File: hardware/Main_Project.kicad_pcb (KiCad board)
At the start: 2 copper layers, 246.8 x 135.9 mm, 64 parts, among them J1 Motors_R, J10 BBBBBBBONUSROUND, J11 Power_Distro, J12 Power_Distro, J13 Power_Distro, J14 Power_Distro, J15 Color_Sensor, J16 Color_Sensor, J2 Motors_L, J3 Power_Outputs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

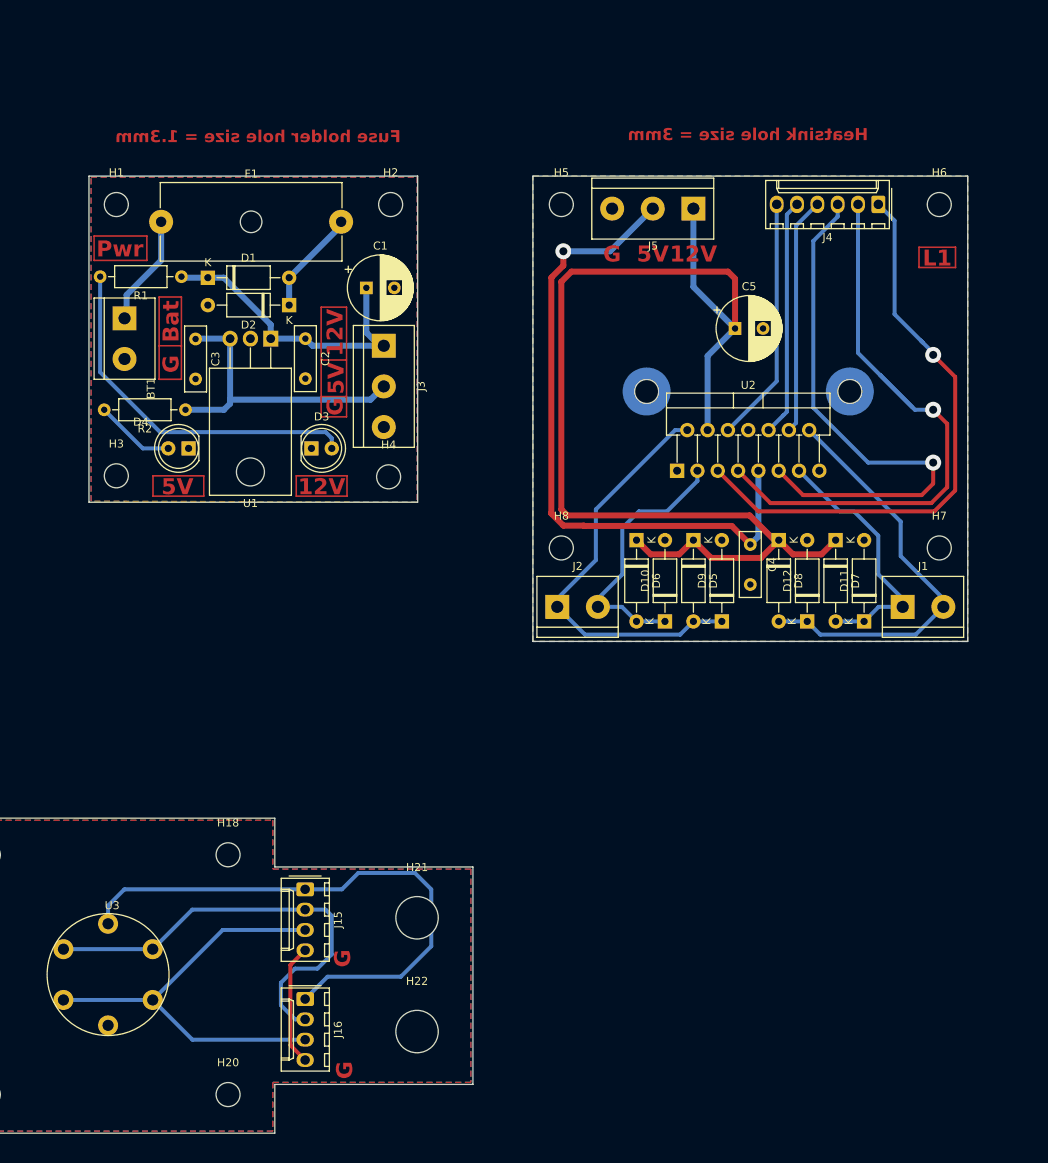
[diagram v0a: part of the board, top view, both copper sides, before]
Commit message: new pcb for magnet
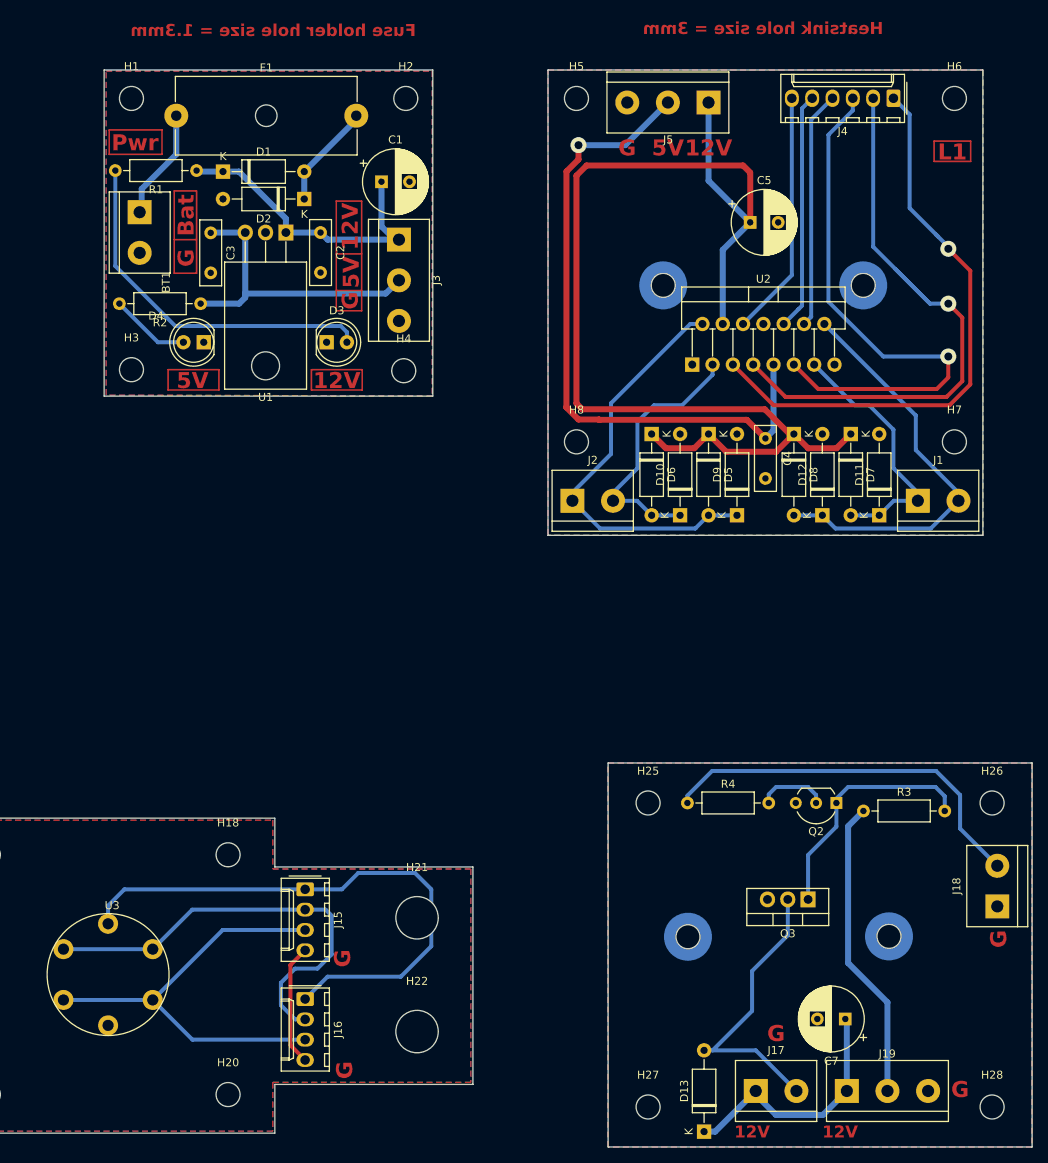
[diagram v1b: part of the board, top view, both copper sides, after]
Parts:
- added C7: 4.7uF, Capacitor_THT:CP_Radial_D8.0mm_P3.50mm, F.Cu at (251.7, 146.0)
- added D13: 1N4004, Diode_THT:D_A-405_P10.16mm_Horizontal, F.Cu at (234.0, 160.1)
- added H25: MountingHole, MountingHole:MountingHole_3mm, F.Cu at (227.0, 119.0)
- added H26: MountingHole, MountingHole:MountingHole_3mm, F.Cu at (270.0, 119.0)
- added H27: MountingHole, MountingHole:MountingHole_3mm, F.Cu at (227.0, 157.0)
- added H28: MountingHole, MountingHole:MountingHole_3mm, F.Cu at (270.0, 157.0)
- added H9: HeatsinkMounting, new_winterbloom:M3_Heatsink_Mounting, F.Cu at (257.1, 135.7)
- added H9: HeatsinkMounting, new_winterbloom:M3_Heatsink_Mounting, F.Cu at (232.0, 135.7)
- added J17: Magnet, TerminalBlock:TerminalBlock_bornier-2_P5.08mm, F.Cu at (240.5, 155.0)
- added J18: FRDM input, TerminalBlock:TerminalBlock_bornier-2_P5.08mm, F.Cu at (270.6, 131.9)
- added J19: Magnet_Power, TerminalBlock:TerminalBlock_bornier-3_P5.08mm, F.Cu at (251.8, 155.0)
- added Q2: BC547, Package_TO_SOT_THT:TO-92_Inline_Wide, F.Cu at (250.5, 119.0)
- added Q3: IRF540N, Package_TO_SOT_THT:TO-220-3_Vertical, F.Cu at (247.0, 131.1)
- added R3: 10k, Resistor_THT:R_Axial_DIN0207_L6.3mm_D2.5mm_P10.16mm_Horizontal, F.Cu at (253.9, 120.0)
- added R4: 1k, Resistor_THT:R_Axial_DIN0207_L6.3mm_D2.5mm_P10.16mm_Horizontal, F.Cu at (231.9, 119.0)
- moved H9 13.4 mm to (228.9, 54.3)
- moved H3 13.4 mm to (162.4, 64.8)
- moved J4 13.4 mm to (257.7, 30.9)
- moved BT1 13.4 mm to (163.4, 45.2)
- moved C1 13.4 mm to (193.7, 41.3)
- moved C2 13.4 mm to (186.1, 47.7)
- moved C3 13.4 mm to (172.3, 47.7)
- moved D1 13.4 mm to (173.9, 40.1)
- moved D3 13.4 mm to (186.8, 61.4)
- moved D4 13.4 mm to (171.5, 61.4)
- moved R1 13.4 mm to (170.6, 39.9)
- moved U1 13.4 mm to (181.7, 47.7)
- moved J5 13.4 mm to (234.6, 31.4)
- moved H1 13.4 mm to (162.4, 30.9)
- moved H2 13.4 mm to (196.7, 30.9)
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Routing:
- net Net-(J18-Pin_2): track 0.00 -> 48.3 mm
- net +5V: track 203.9 -> 241.8 mm
- net Net-(D13-A): track 0.00 -> 36.4 mm
- net +12V: track 285.9 -> 317.7 mm
- net Net-(Q2-C): track 0.00 -> 30.5 mm
- net Net-(Q2-B): track 0.00 -> 8.80 mm
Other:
- board size 246.8 x 135.9 mm -> 254.8 x 137.6 mm
